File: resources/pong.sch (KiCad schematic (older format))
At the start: 23 parts, among them J1 RCA_JACK, J2 RCA_JACK, Q1 2N3904, SW1 SPST, SW2 left up, SW3 left down, SW4 right up, SW5 right down, U1 PIC10F322

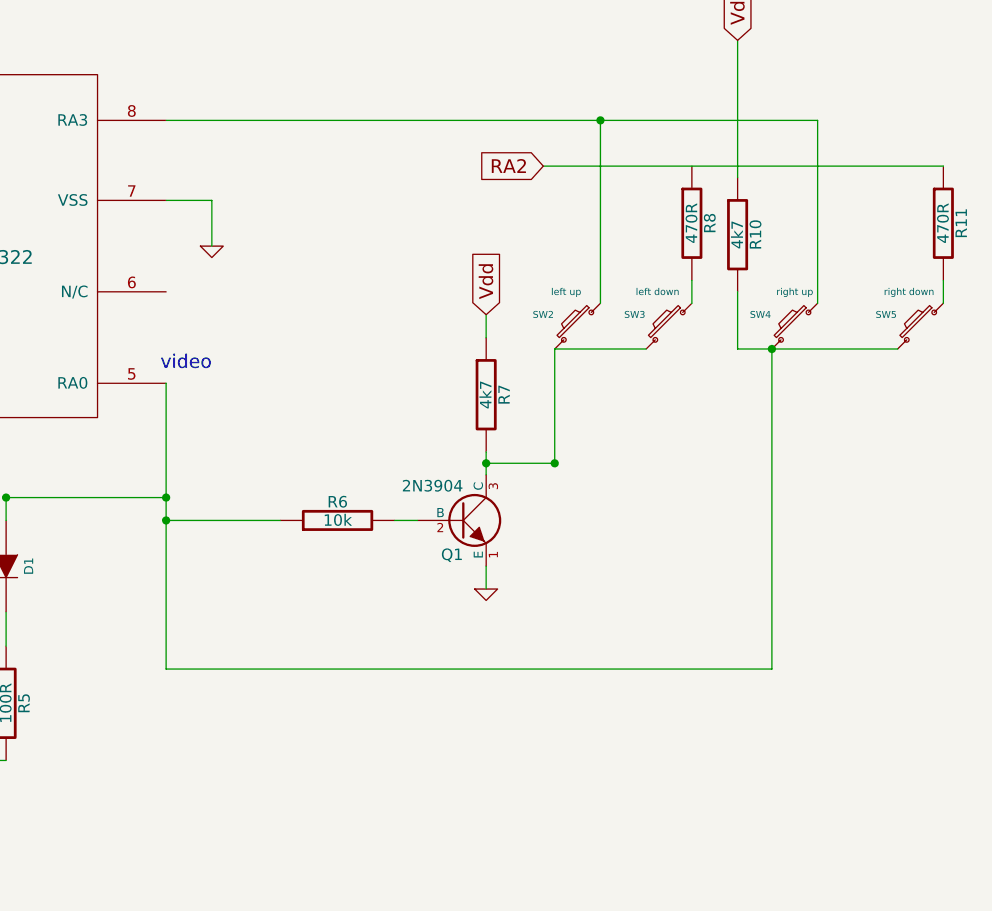
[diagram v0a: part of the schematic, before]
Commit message: modification au circuit, remplacé vidéo
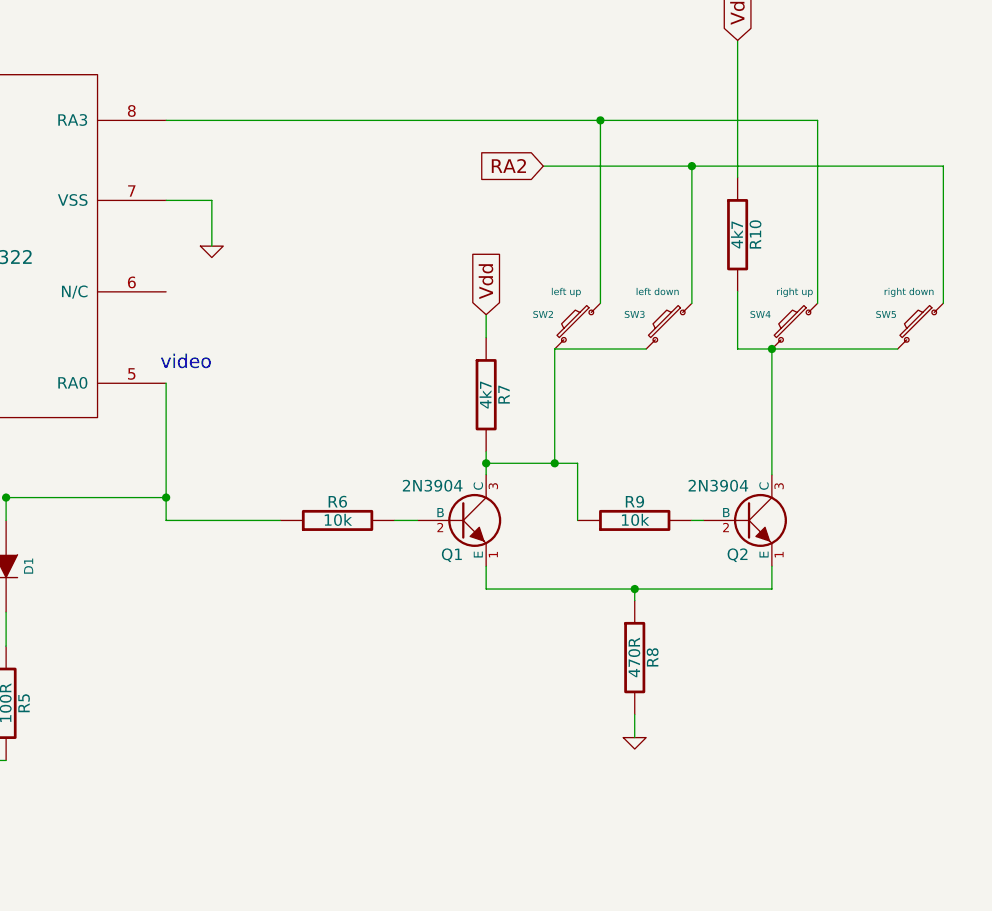
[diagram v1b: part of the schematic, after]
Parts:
- removed R11: 470R, symbol R
- added Q2: 2N3904, symbol NPN
- added R9: 10k, symbol R
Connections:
- net GND: now also R8.2; no longer Q1.1 (E)
- net RA2: now also SW3.1, SW5.1
- net at D1.1 (A), R6.1, U1.5 (RA0): no longer R10.2, SW4.2, SW5.2
- net at Q1.3 (C), R7.2, SW2.2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: now also R9.1
- net at R8.1: now also Q1.1 (E), Q2.1 (E)
- new net: Q2.2 (B), R9.2
- new net: Q2.3 (C), R10.2, SW4.2, SW5.2
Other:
- moved on the sheet: R8
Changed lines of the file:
@@
-EESchema Schematic File Version 2  date 2013-08-17 23:34:59
+EESchema Schematic File Version 2  date 2013-08-18 09:13:30
 LIBS:power
 LIBS:device
@@
 	1    0    0    -1
 $EndComp
-Wire Wire Line
-	4700 4250 4700 5100
-Wire Wire Line
-	5600 5300 5600 5450
-Wire Wire Line
-	4700 5600 4700 5950
-Wire Wire Line
-	4700 5950 5600 5950
-Wire Wire Line
-	4350 6450 4350 6550
-Wire Wire Line
-	3000 3900 3300 3900
-Wire Wire Line
-	6300 3500 6500 3500
-Wire Wire Line
-	6500 3500 6500 3700
-Wire Wire Line
-	3000 4400 3000 4500
-Connection ~ 2650 4400
-Wire Wire Line
-	4500 3500 4700 3500
-Wire Wire Line
-	1550 2250 1700 2250
-Wire Wire Line
-	2700 2000 2700 2350
-Connection ~ 2700 2250
-Wire Wire Line
-	2700 2250 3250 2250
-Wire Wire Line
-	3250 2250 3250 2350
-Wire Wire Line
-	3250 2750 3250 2950
-Wire Wire Line
-	2700 2750 2700 2950
-Wire Wire Line
-	1550 2850 1550 3000
-Wire Wire Line
-	5600 4900 5600 4800
-Connection ~ 5600 4800
-Connection ~ 4700 4600
 Text Notes 6500 4250 2    60   ~ 0
 video
@@
 Text Notes 6700 2500 2    197  ~ 0
 pong game
-Wire Wire Line
-	6300 4300 6300 5550
 Text GLabel 4000 3650 1    60   Input ~ 0
 RA2
-Wire Wire Line
-	4000 3900 4000 3650
-Connection ~ 4000 3900
-Wire Wire Line
-	3800 3900 4700 3900
-Connection ~ 3000 4400
-Connection ~ 3250 3900
 $Comp
 L NPN Q1
@@
 F 3 "" H 7600 4900 60  0000 C CNN
 	1    7600 4900
-	1    0    0    -1
-$EndComp
-$Comp
-L GND #PWR7
-U 1 1 520CE5FE
-P 7700 5200
-F 0 "#PWR7" H 7700 5200 30  0001 C CNN
-F 1 "GND" H 7700 5130 30  0001 C CNN
-F 2 "" H 7700 5200 60  0000 C CNN
-F 3 "" H 7700 5200 60  0000 C CNN
-	1    7700 5200
 	1    0    0    -1
 $EndComp
@@
 	0    -1   -1   0
 $EndComp
-Wire Wire Line
-	7700 5100 7700 5200
-Wire Wire Line
-	7300 4900 7400 4900
-Wire Wire Line
-	7700 4600 7700 4700
-Connection ~ 7700 4650
-Wire Wire Line
-	6300 4900 6800 4900
 Text GLabel 7700 4000 1    60   Input ~ 0
 Vdd
-Wire Wire Line
-	7700 4100 7700 4000
 $Comp
 L SW_PUSH_SMALL SW2
@@
 	-1   0    0    -1
 $EndComp
-Wire Wire Line
-	8950 4150 8950 5550
-Wire Wire Line
-	8800 4150 9500 4150
-Wire Wire Line
-	8400 4150 8000 4150
-Wire Wire Line
-	8000 4150 8000 4650
-Connection ~ 8000 4650
 $Comp
 L R R8
 U 1 1 520CE9E9
-P 8600 3600
-F 0 "R8" V 8680 3600 50  0000 C CNN
-F 1 "470R" V 8600 3600 50  0000 C CNN
-F 2 "" H 8600 3600 60  0000 C CNN
-F 3 "" H 8600 3600 60  0000 C CNN
-	1    8600 3600
-	1    0    0    -1
-$EndComp
-$Comp
-L R R11
-U 1 1 520CE9EF
-P 9700 3600
-F 0 "R11" V 9780 3600 50  0000 C CNN
-F 1 "470R" V 9700 3600 50  0000 C CNN
-F 2 "" H 9700 3600 60  0000 C CNN
-F 3 "" H 9700 3600 60  0000 C CNN
-	1    9700 3600
-	1    0    0    -1
-$EndComp
-Wire Wire Line
-	8200 3150 8200 3950
-Wire Wire Line
-	9150 3150 9150 3950
+P 8350 5500
+F 0 "R8" V 8430 5500 50  0000 C CNN
+F 1 "470R" V 8350 5500 50  0000 C CNN
+F 2 "" H 8350 5500 60  0000 C CNN
+F 3 "" H 8350 5500 60  0000 C CNN
+	1    8350 5500
+	1    0    0    -1
+$EndComp
 Text GLabel 7950 3350 0    60   Input ~ 0
 RA2
-Wire Wire Line
-	7950 3350 9700 3350
 $Comp
 L R R3
@@
 	1    0    0    -1
 $EndComp
-Wire Wire Line
-	3800 3900 3800 3800
 $Comp
 L R R10
@@
 	1    0    0    -1
 $EndComp
+Text GLabel 8800 2800 1    60   Input ~ 0
+Vdd
+Text GLabel 3800 3150 1    60   Input ~ 0
+Vdd
+Text Notes 7500 7550 0    60   ~ 0
+pong game\n
+Wire Wire Line
+	4700 4250 4700 5100
+Wire Wire Line
+	5600 5300 5600 5450
+Wire Wire Line
+	4700 5600 4700 5950
+Wire Wire Line
+	4700 5950 5600 5950
+Wire Wire Line
+	4350 6450 4350 6550
+Wire Wire Line
+	3000 3900 3300 3900
+Wire Wire Line
+	6300 3500 6500 3500
+Wire Wire Line
+	6500 3500 6500 3700
+Wire Wire Line
+	3000 4400 3000 4500
+Connection ~ 2650 4400
+Wire Wire Line
+	4500 3500 4700 3500
+Wire Wire Line
+	1550 2250 1700 2250
+Wire Wire Line
+	2700 2000 2700 2350
+Connection ~ 2700 2250
+Wire Wire Line
+	2700 2250 3250 2250
+Wire Wire Line
+	3250 2250 3250 2350
+Wire Wire Line
+	3250 2750 3250 2950
+Wire Wire Line
+	2700 2750 2700 2950
+Wire Wire Line
+	1550 2850 1550 3000
+Wire Wire Line
+	5600 4900 5600 4800
+Connection ~ 5600 4800
+Connection ~ 4700 4600
+Wire Wire Line
+	6300 4300 6300 4900
+Wire Wire Line
+	4000 3900 4000 3650
+Connection ~ 4000 3900
+Wire Wire Line
+	3800 3900 4700 3900
+Connection ~ 3000 4400
+Connection ~ 3250 3900
+Wire Wire Line
+	7700 5100 7700 5200
+Wire Wire Line
+	7300 4900 7400 4900
+Wire Wire Line
+	7700 4600 7700 4700
+Connection ~ 7700 4650
+Wire Wire Line
+	6300 4900 6800 4900
+Wire Wire Line
+	7700 4100 7700 4000
+Wire Wire Line
+	8950 4700 8950 4150
+Wire Wire Line
+	8800 4150 9500 4150
+Wire Wire Line
+	8400 4150 8000 4150
+Wire Wire Line
+	8000 4150 8000 4650
+Connection ~ 8000 4650
+Wire Wire Line
+	8200 3150 8200 3950
+Wire Wire Line
+	9150 3150 9150 3950
+Wire Wire Line
+	7950 3350 9700 3350
+Wire Wire Line
+	3800 3900 3800 3800
 Wire Wire Line
 	8800 3900 8800 4150
 Connection ~ 8950 4150
-Text GLabel 8800 2800 1    60   Input ~ 0
-Vdd
 Wire Wire Line
 	8800 2800 8800 3400
 Wire Wire Line
 	2650 4400 3000 4400
-Text GLabel 3800 3150 1    60   Input ~ 0
-Vdd
 Wire Wire Line
 	3800 3300 3800 3150
@@
 	5600 4800 6300 4800
 Connection ~ 6300 4800
-Text Notes 7500 7550 0    60   ~ 0
-pong game\n
 Wire Wire Line
 	6300 3150 9150 3150
 Connection ~ 8200 3150
 Wire Wire Line
-	8600 3850 8600 3950
-Wire Wire Line
-	9700 3850 9700 3950
-Wire Wire Line
-	8000 4650 7700 4650
-Wire Wire Line
-	8950 5550 6300 5550
-Connection ~ 6300 4900
+	8600 3350 8600 3950
+Wire Wire Line
+	9700 3350 9700 3950
+Wire Wire Line
+	8100 4650 7700 4650
+Wire Wire Line
+	8100 4900 8100 4650
+Wire Wire Line
+	8600 4900 8650 4900
+$Comp
+L R R9
+U 1 1 520CE635
+P 8350 4900
+F 0 "R9" V 8430 4900 50  0000 C CNN
+F 1 "10k" V 8350 4900 50  0000 C CNN
+F 2 "" H 8350 4900 60  0000 C CNN
+F 3 "" H 8350 4900 60  0000 C CNN
+	1    8350 4900
+	0    -1   -1   0
+$EndComp
+Wire Wire Line
+	8950 5100 8950 5200
+$Comp
+L NPN Q2
+U 1 1 520CE5F4
+P 8850 4900
+F 0 "Q2" H 8850 4750 50  0000 R CNN
+F 1 "2N3904" H 8850 5050 50  0000 R CNN
+F 2 "" H 8850 4900 60  0000 C CNN
+F 3 "" H 8850 4900 60  0000 C CNN
+	1    8850 4900
+	1    0    0    -1
+$EndComp
+Wire Wire Line
+	8950 5200 7700 5200
+Wire Wire Line
+	8350 5250 8350 5200
+Connection ~ 8350 5200
+$Comp
+L GND #PWR?
+U 1 1 5210C4D7
+P 8350 5850
+F 0 "#PWR?" H 8350 5850 30  0001 C CNN
+F 1 "GND" H 8350 5780 30  0001 C CNN
+F 2 "" H 8350 5850 60  0000 C CNN
+F 3 "" H 8350 5850 60  0000 C CNN
+	1    8350 5850
+	1    0    0    -1
+$EndComp
+Wire Wire Line
+	8350 5750 8350 5850
+Connection ~ 8600 3350
 $EndSCHEMATC

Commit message: modification projet kicad
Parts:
- R8: value 470R -> 1K
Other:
- moved on the sheet: BT1, C1, C2, SW1
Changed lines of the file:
@@
-EESchema Schematic File Version 2  date 2013-08-18 09:13:30
+EESchema Schematic File Version 2  date 2013-08-18 12:42:24
 LIBS:power
 LIBS:device
@@
 L BATTERY BT1
 U 1 1 520AB93E
-P 1550 2550
-F 0 "BT1" H 1550 2750 50  0000 C CNN
-F 1 "3Volt" H 1550 2360 50  0000 C CNN
-F 2 "" H 1550 2550 60  0000 C CNN
-F 3 "" H 1550 2550 60  0000 C CNN
-	1    1550 2550
+P 1500 2700
+F 0 "BT1" H 1500 2900 50  0000 C CNN
+F 1 "3Volt" H 1500 2510 50  0000 C CNN
+F 2 "" H 1500 2700 60  0000 C CNN
+F 3 "" H 1500 2700 60  0000 C CNN
+	1    1500 2700
 	0    1    1    0
 $EndComp
-Text GLabel 2700 2000 1    60   Input ~ 0
+Text GLabel 2650 2150 1    60   Input ~ 0
 Vdd
 $Comp
 L SPST SW1
 U 1 1 520AB976
-P 2200 2250
-F 0 "SW1" H 2200 2350 70  0000 C CNN
-F 1 "SPST" H 2200 2150 70  0000 C CNN
-F 2 "" H 2200 2250 60  0000 C CNN
-F 3 "" H 2200 2250 60  0000 C CNN
-	1    2200 2250
+P 2150 2400
+F 0 "SW1" H 2150 2500 70  0000 C CNN
+F 1 "SPST" H 2150 2300 70  0000 C CNN
+F 2 "" H 2150 2400 60  0000 C CNN
+F 3 "" H 2150 2400 60  0000 C CNN
+	1    2150 2400
 	1    0    0    -1
 $EndComp
@@
 L GND #PWR1
 U 1 1 520AB985
-P 1550 3000
-F 0 "#PWR1" H 1550 3000 30  0001 C CNN
-F 1 "GND" H 1550 2930 30  0001 C CNN
-F 2 "" H 1550 3000 60  0000 C CNN
-F 3 "" H 1550 3000 60  0000 C CNN
-	1    1550 3000
+P 1500 3150
+F 0 "#PWR1" H 1500 3150 30  0001 C CNN
+F 1 "GND" H 1500 3080 30  0001 C CNN
+F 2 "" H 1500 3150 60  0000 C CNN
+F 3 "" H 1500 3150 60  0000 C CNN
+	1    1500 3150
 	1    0    0    -1
 $EndComp
@@
 L C C1
 U 1 1 520AB98D
-P 2700 2550
-F 0 "C1" H 2750 2650 50  0000 L CNN
-F 1 "100nF" H 2750 2450 50  0000 L CNN
-F 2 "" H 2700 2550 60  0000 C CNN
-F 3 "" H 2700 2550 60  0000 C CNN
-	1    2700 2550
+P 2650 2700
+F 0 "C1" H 2700 2800 50  0000 L CNN
+F 1 "100nF" H 2700 2600 50  0000 L CNN
+F 2 "" H 2650 2700 60  0000 C CNN
+F 3 "" H 2650 2700 60  0000 C CNN
+	1    2650 2700
 	1    0    0    -1
 $EndComp
@@
 L C C2
 U 1 1 520AB99A
-P 3250 2550
-F 0 "C2" H 3300 2650 50  0000 L CNN
-F 1 "10µF" H 3300 2450 50  0000 L CNN
-F 2 "" H 3250 2550 60  0000 C CNN
-F 3 "" H 3250 2550 60  0000 C CNN
-	1    3250 2550
+P 3200 2700
+F 0 "C2" H 3250 2800 50  0000 L CNN
+F 1 "10µF" H 3250 2600 50  0000 L CNN
+F 2 "" H 3200 2700 60  0000 C CNN
+F 3 "" H 3200 2700 60  0000 C CNN
+	1    3200 2700
 	1    0    0    -1
 $EndComp
@@
 L GND #PWR3
 U 1 1 520AB9A0
-P 2700 2950
-F 0 "#PWR3" H 2700 2950 30  0001 C CNN
-F 1 "GND" H 2700 2880 30  0001 C CNN
-F 2 "" H 2700 2950 60  0000 C CNN
-F 3 "" H 2700 2950 60  0000 C CNN
-	1    2700 2950
+P 2650 3100
+F 0 "#PWR3" H 2650 3100 30  0001 C CNN
+F 1 "GND" H 2650 3030 30  0001 C CNN
+F 2 "" H 2650 3100 60  0000 C CNN
+F 3 "" H 2650 3100 60  0000 C CNN
+	1    2650 3100
 	1    0    0    -1
 $EndComp
@@
 L GND #PWR4
 U 1 1 520AB9A6
-P 3250 2950
-F 0 "#PWR4" H 3250 2950 30  0001 C CNN
-F 1 "GND" H 3250 2880 30  0001 C CNN
-F 2 "" H 3250 2950 60  0000 C CNN
-F 3 "" H 3250 2950 60  0000 C CNN
-	1    3250 2950
+P 3200 3100
+F 0 "#PWR4" H 3200 3100 30  0001 C CNN
+F 1 "GND" H 3200 3030 30  0001 C CNN
+F 2 "" H 3200 3100 60  0000 C CNN
+F 3 "" H 3200 3100 60  0000 C CNN
+	1    3200 3100
 	1    0    0    -1
 $EndComp
@@
 P 8350 5500
 F 0 "R8" V 8430 5500 50  0000 C CNN
-F 1 "470R" V 8350 5500 50  0000 C CNN
+F 1 "1K" V 8350 5500 50  0000 C CNN
 F 2 "" H 8350 5500 60  0000 C CNN
 F 3 "" H 8350 5500 60  0000 C CNN
@@
 	4500 3500 4700 3500
 Wire Wire Line
-	1550 2250 1700 2250
-Wire Wire Line
-	2700 2000 2700 2350
-Connection ~ 2700 2250
-Wire Wire Line
-	2700 2250 3250 2250
-Wire Wire Line
-	3250 2250 3250 2350
-Wire Wire Line
-	3250 2750 3250 2950
-Wire Wire Line
-	2700 2750 2700 2950
-Wire Wire Line
-	1550 2850 1550 3000
+	1500 2400 1650 2400
+Wire Wire Line
+	2650 2150 2650 2500
+Connection ~ 2650 2400
+Wire Wire Line
+	2650 2400 3200 2400
+Wire Wire Line
+	3200 2400 3200 2500
+Wire Wire Line
+	3200 2900 3200 3100
+Wire Wire Line
+	2650 2900 2650 3100
+Wire Wire Line
+	1500 3000 1500 3150
 Wire Wire Line
 	5600 4900 5600 4800
